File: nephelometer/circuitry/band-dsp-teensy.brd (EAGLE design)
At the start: 74 x 55 mm, 40 parts, among them IC1 LM4041CILP, IC2 AD822N, IC3 MCP6S21, J1 RJ11-6PTH, Q1 IRLB8721, T1 2N2222, T2 2N2222

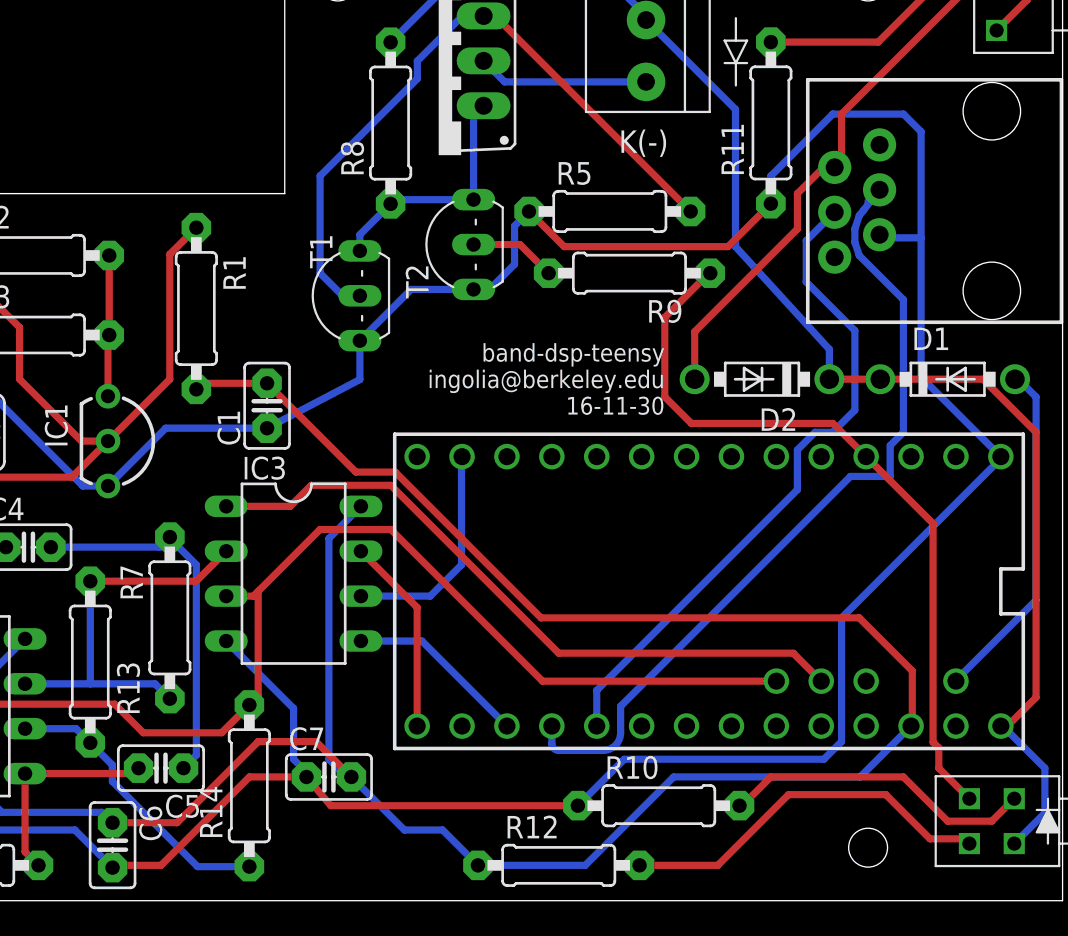
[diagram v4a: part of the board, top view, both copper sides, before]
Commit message: Motor control with transistor gating MOSFET, shutoff when disconnected
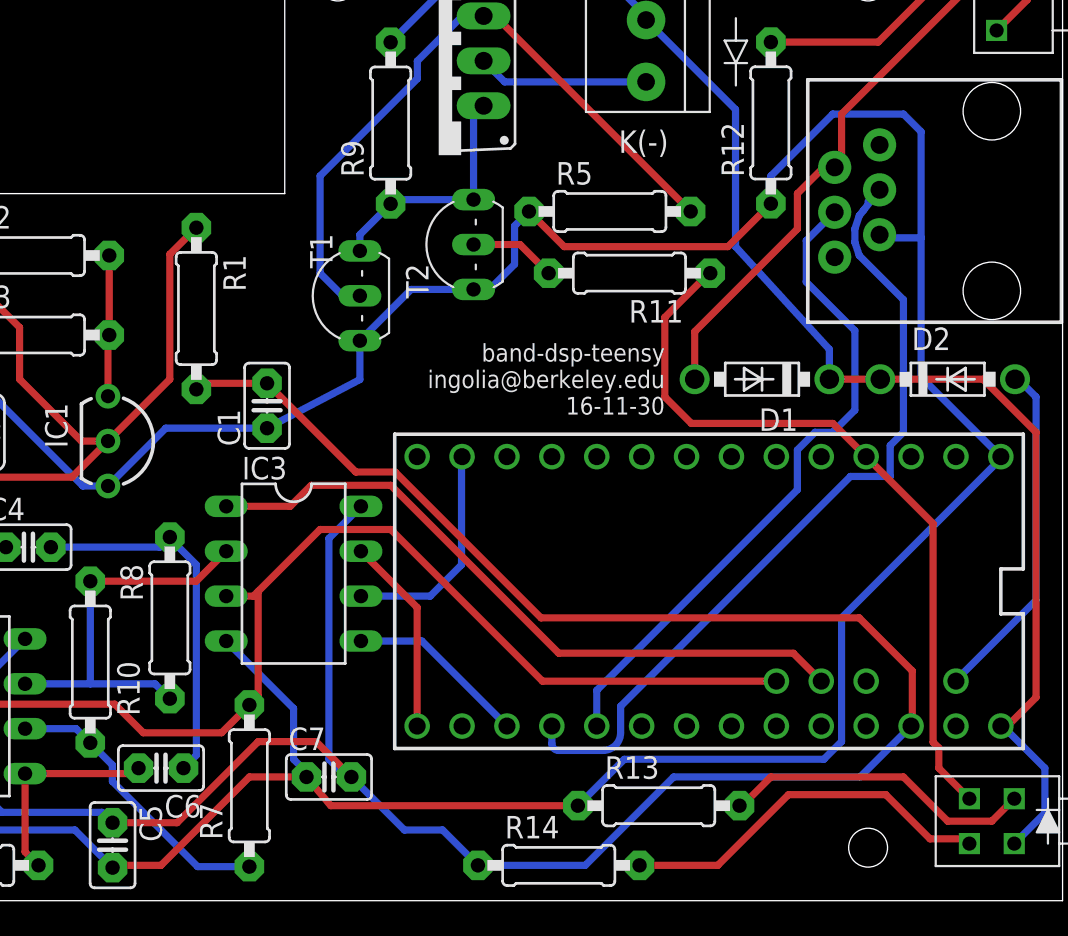
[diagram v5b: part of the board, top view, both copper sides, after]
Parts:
- C5: value 1.2pF -> 100nF
- C6: value 100nF -> 1.2pF
- R10: value 330R -> 14K3
- R11: value 330R -> 4K7
- R12: value 150R -> 330R
- R13: value 14K3 -> 330R
- R14: value 14K3 -> 150R
- R8: value 4K7 -> 14K3
- moved R12 43.7 mm to (57.5, 49.0), turned to 90 degrees
- moved R10 33.2 mm to (19.0, 18.5), turned to 270 degrees
- moved R13 33.2 mm to (51.2, 10.4), turned to 0 degrees
- moved R8 30.7 mm to (23.5, 21.0)
- moved R14 18.1 mm to (45.5, 7.00), turned to 0 degrees
- moved R9 16.0 mm to (36.0, 49.0), turned to 90 degrees
- moved R11 11.7 mm to (49.5, 40.5), turned to 180 degrees
- moved R7 10.5 mm to (28.0, 11.5)
- moved D1 10.5 mm to (57.0, 34.5), turned to 180 degrees
- moved D2 10.5 mm to (67.5, 34.5), turned to 0 degrees
- moved C5 5.15 mm to (20.3, 8.14), turned to 270 degrees
- moved C6 5.15 mm to (23.0, 12.5), turned to 180 degrees
- renumbered JP1 to LED1, U$5 to LED3, U$6 to LED2
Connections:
- net +3V3: now also C5.1, R14.1; no longer C6.1, R12.1
- net +5V: now also R9.2; no longer R8.2
- net 1V65: now also R7.2; no longer R14.2
- net GND: now also C5.2, R12.1, R13.1; no longer C6.2, R10.1, R11.1
- net LEDCTRL: now also R11.2; no longer R9.2
- net N$10: now also D1.A; no longer D2.A
- net N$11: now also R14.2; no longer R12.2
- net N$12: now also R12.2; no longer R11.2
- net N$2: now also C6.1, R8.2; no longer C5.1, R7.2
- net N$3: now also R10.1, R8.1; no longer R13.1, R7.1
- net N$5: now also R11.1; no longer R9.1
- net N$6: now also R10.2, R7.1; no longer R13.2, R14.1
- net N$7: now also R13.2; no longer R10.2
- net N$8: now also R9.1; no longer R8.1
- net N$9: now also C6.2; no longer C5.2
- net V+: now also D2.A; no longer D1.A

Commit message: Corrected resistor divider
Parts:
- R2: value 1K00 -> 3K01
- R3: value 3K01 -> 1K00
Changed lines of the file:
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@@
 <?xml version="1.0" encoding="utf-8"?>
 <!DOCTYPE eagle SYSTEM "eagle.dtd">
-<eagle version="7.5.0">
+<eagle version="7.7.0">
 <drawing>
 <settings>
@@
 <attribute name="MANF#" value="IRLB8721PBF" x="41.25" y="52.51" size="1.778" layer="27" rot="R90" display="off"/>
 </element>
-<element name="R2" library="adafruit" package="0207/9" value="1K00" x="15.5" y="41.5">
+<element name="R2" library="adafruit" package="0207/9" value="3K01" x="15.5" y="41.5">
 <attribute name="DIGIKEY#" value="RNF14FTD1K00CT-ND" x="15.5" y="41.5" size="1.778" layer="27" display="off"/>
 <attribute name="MANF" value="Stackpole Electronics Inc." x="15.5" y="41.5" size="1.778" layer="27" display="off"/>
@@
 <element name="U$2" library="ingolia" package="M2MOUNT" value="" x="63" y="57"/>
 <element name="U$3" library="ingolia" package="M2MOUNT" value="" x="63" y="8"/>
-<element name="R3" library="adafruit" package="0207/9" value="3K01" x="15.5" y="37">
+<element name="R3" library="adafruit" package="0207/9" value="1K00" x="15.5" y="37">
 <attribute name="DIGIKEY#" value="RNF14FTD3K01CT-ND" x="15.5" y="37" size="1.778" layer="27" display="off"/>
 <attribute name="MANF" value="Stackpole Electronics Inc." x="15.5" y="37" size="1.778" layer="27" display="off"/>

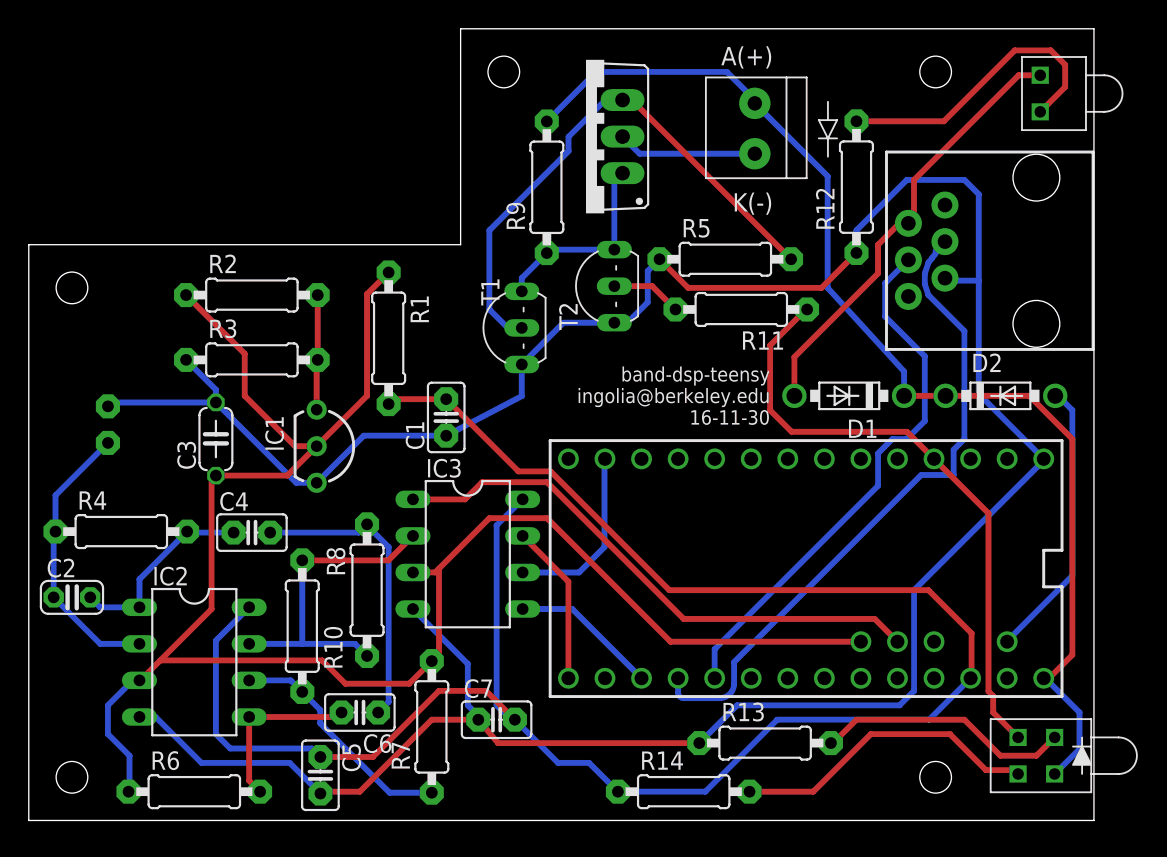
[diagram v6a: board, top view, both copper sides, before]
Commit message: Revised detector board circuit, picked filter values, finalized parts
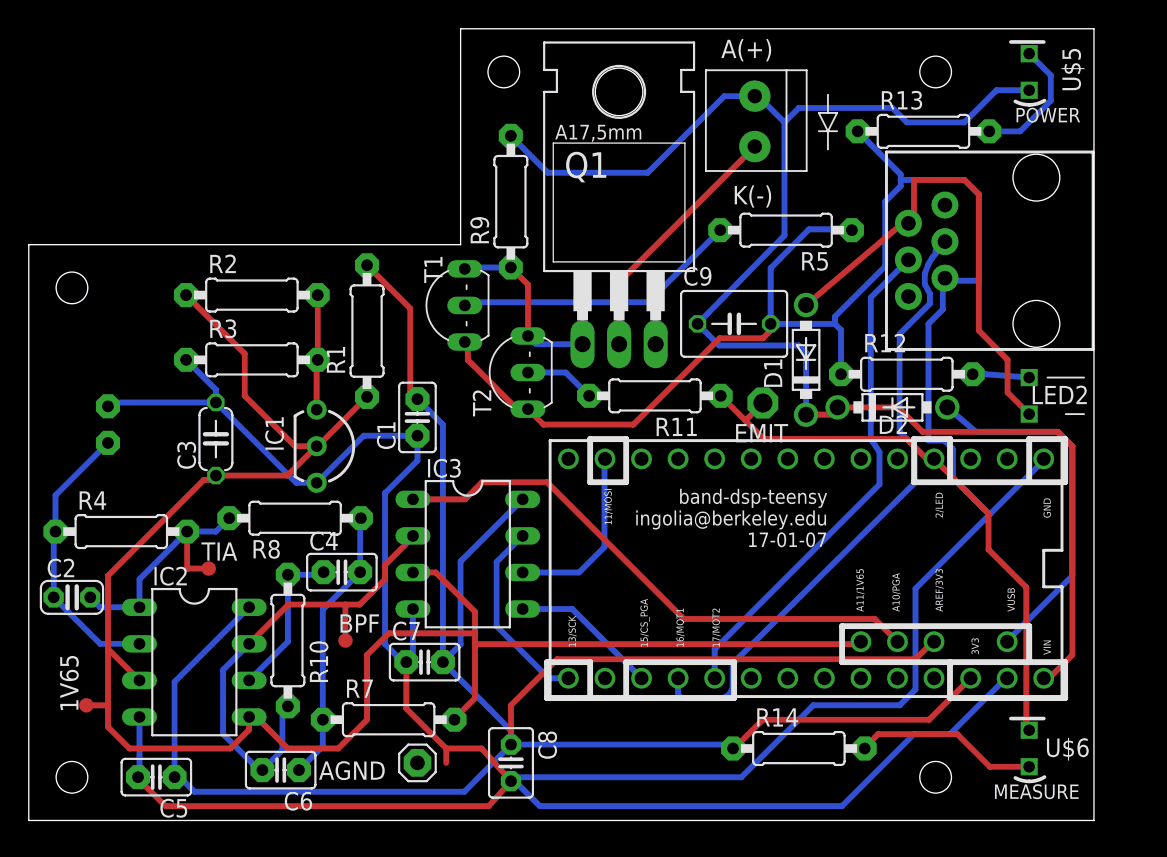
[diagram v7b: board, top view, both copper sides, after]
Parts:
- removed LED3: LED3MM-BILEV-INDIC, ingolia:LED3MM-BILEV-INDIC
- removed R6: 28k7, adafruit:0207/9
- added 1V65, BPF, TIA: TPTP10R, testpad:TP10R
- added AGND: (no value), adafruit:1X01
- added C8: 10µF, adafruit:C025-030X050
- added C9: 22µF, adafruit:C050-045X075
- added EMIT: TPPAD1-13, testpad:P1-13
- added U$5, U$6: LED3MM_H101C, ingolia:LED3MM_H101C
- C4, C6: value 1.2pF -> 1.2nF
- LED2: value LED3MM-RG-INDIC -> LED3MM_WP937EGW; device ingolia:LED3MM-INDIC -> ingolia:LED3MM_H101C_BICOL
- Q1: device ingolia:TO220BV -> ingolia:TO220BH
- R10: value 14K3 -> 133K
- R14: value 150R -> 330R
- R7: value 14K3 -> 1K47
- R8: value 14K3 -> 13K3
- moved R13 43.9 mm to (62.2, 52.9)
- moved LED2 21.0 mm to (69.5, 34.5)
- moved R12 13.5 mm to (61.0, 36.0), turned to 0 degrees
- moved C5 11.4 mm to (8.86, 8.01), turned to 180 degrees
- moved R14 8.54 mm to (53.5, 10.0)
- moved R11 8.49 mm to (43.5, 34.5)
- moved T2 8.49 mm to (33.4, 36.1)
- moved D2 7.54 mm to (60.0, 33.7)
- moved R8 7.07 mm to (18.5, 26.0), turned to 180 degrees
- moved C4 6.83 mm to (21.8, 22.2)
- moved C6 6.80 mm to (17.5, 8.50)
- moved C7 6.40 mm to (27.5, 16.0)
- moved R5 4.68 mm to (52.6, 46.0), turned to 180 degrees
- moved Q1 4.27 mm to (41.0, 48.2), turned to 0 degrees
- moved T1 4.26 mm to (29.0, 40.8)
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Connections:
- removed net AGND: BRD1.AGND
- removed net AREF: BRD1.AREF
- removed net N$2: C4.2, C6.1, R8.2
- net +3V3: now also BRD1.AREF, C8.1
- net +5V: now also C9.1, U$5.A; no longer LED3.AB
- net 1V65: now also 1V65.TP, IC2.5; no longer R6.1
- net GND: now also AGND.1, BRD1.AGND, C8.2, C9.2
- net N$10: now also LED2.SHORT; no longer LED2.1
- net N$11: now also U$6.A; no longer LED3.AT
- net N$12: now also LED2.LONG; no longer LED2.2
- net N$22: now also R8.2, TIA.TP; no longer C4.1
- net N$3: now also C4.2, C6.1, R7.1; no longer IC2.7, IC3.2, R10.1
- net N$5: now also EMIT.TP, U$6.K; no longer LED3.CT
- net N$6: now also BPF.TP, C6.2, IC2.7, IC3.2; no longer IC2.6, R7.1
- net N$7: now also U$5.K; no longer LED3.CB
- net N$9: now also C4.1, IC2.6, R10.1; no longer C6.2, IC2.5, R6.2
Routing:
- net GND: track 193.5 -> 281.8 mm
- net +5V: track 80.4 -> 108.2 mm
- net N$2: track 21.0 -> 0.00 mm
- net +3V3: track 138.2 -> 158.2 mm
- net N$6: track 16.5 -> 33.6 mm
- net N$12: track 20.9 -> 3.94 mm
- net N$14: track 38.2 -> 23.1 mm
- net N$7: track 17.8 -> 9.04 mm
- net N$11: track 21.5 -> 12.8 mm
- net N$18: track 9.68 -> 17.6 mm
- net V+: track 19.6 -> 25.2 mm
- net N$22: track 13.6 -> 17.8 mm
- net N$10: track 30.6 -> 34.1 mm
- net N$3: track 22.7 -> 19.3 mm
- net N$5: track 42.7 -> 40.2 mm
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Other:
- board text added: "11/MOSI"
- board text added: "13/SCK"
- board text added: "15/CS_PGA"
- board text added: "16/MOT1"
- board text added: "17/MOT2"
- board text added: "2/LED"
- board text added: "3V3"
- board text added: "A10/PGA"
- board text added: "A11/1V65"
- board text added: "AREF/3V3"
- board text added: "GND"
- board text added: "MEASURE"
- board text added: "POWER"
- board text added: "VIN"
- board text added: "VUSB"
- board text added: "band-dsp-teensy ingolia@berkeley.edu 17-01-07"
- board text removed: "band-dsp-teensy ingolia@berkeley.edu 16-11-30"

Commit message: Finalized parts and components for 10kHz band-pass etc
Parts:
- R7: value 1K47 -> 1K65
- R8: value 13K3 -> 6K65
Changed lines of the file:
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@@
 <attribute name="MANF" value="Vishay BC Components" x="17.5" y="8.5" size="1.778" layer="27" rot="R180" display="off"/>
 </element>
-<element name="R8" library="adafruit" package="0207/9" value="13K3" x="18.5" y="26" smashed="yes" rot="R180">
-<attribute name="DIGIKEY#" value="13.3KXBK-ND" x="18.5" y="26" size="1.778" layer="27" rot="R180" display="off"/>
+<element name="R8" library="adafruit" package="0207/9" value="6K65" x="18.5" y="26" smashed="yes" rot="R180">
+<attribute name="DIGIKEY#" value="6.65KXBK-ND" x="18.5" y="26" size="1.778" layer="27" rot="R180" display="off"/>
 <attribute name="MANF" value="Yageo" x="18.5" y="26" size="1.778" layer="27" rot="R180" display="off"/>
-<attribute name="MANF#" value="MFR-25FBF52-13K3" x="18.5" y="26" size="1.778" layer="27" rot="R180" display="off"/>
+<attribute name="MANF#" value="MFR-25FBF52-6K65" x="18.5" y="26" size="1.778" layer="27" rot="R180" display="off"/>
 <attribute name="NAME" x="17.548" y="24.476" size="1.27" layer="25" ratio="10" rot="R180"/>
 <attribute name="VALUE" x="20.7606" y="26.635" size="1.27" layer="27" ratio="10" rot="R180"/>
@@
 <attribute name="VALUE" x="17.365" y="19.7606" size="1.27" layer="27" ratio="10" rot="R270"/>
 </element>
-<element name="R7" library="adafruit" package="0207/9" value="1K47" x="25" y="12">
-<attribute name="MANF#" value="MFR-25FBF52-1K5" x="25" y="12" size="1.778" layer="27" display="off"/>
+<element name="R7" library="adafruit" package="0207/9" value="1K65" x="25" y="12">
+<attribute name="MANF#" value="MFR-25FBF52-1K65" x="25" y="12" size="1.778" layer="27" display="off"/>
 <attribute name="MANF" value="Yageo" x="25" y="12" size="1.778" layer="27" display="off"/>
-<attribute name="DIGIKEY#" value="1.50KXBK-ND" x="25" y="12" size="1.778" layer="27" display="off"/>
+<attribute name="DIGIKEY#" value="1.65KXBK-ND" x="25" y="12" size="1.778" layer="27" display="off"/>
 </element>
 <element name="C8" library="adafruit" package="C025-030X050" value="10µF" x="33.5" y="9" rot="R270">
@@
 <wire x1="29" y1="9" x2="29" y2="10" width="0.4064" layer="1"/>
 <contactref element="AGND" pad="1"/>
-<wire x1="27" y1="9" x2="9.5" y2="6" width="0" layer="19" extent="1-1"/>
+<wire x1="29" y1="9" x2="27" y2="9" width="0" layer="19" extent="1-16"/>
 </signal>
 <signal name="N$1">
